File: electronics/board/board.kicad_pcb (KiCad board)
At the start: 2 copper layers, 196.2 x 40.6 mm, 82 parts, among them J1 Screw_Terminal_01x02, J10 Conn_01x02, J11 Conn_01x02, J12 Conn_01x02, J13 Conn_01x02, J14 Conn_01x02, J15 Conn_01x02, J16 Conn_01x02, J17 Conn_01x02, J18 Conn_01x02, J19 Conn_01x02, J2 Screw_Terminal_01x02, J20 Conn_01x02, J21 Conn_01x02, J22 Conn_01x02, J23 Conn_01x02, J3 AVR-ISP-6, J4 USB_B_Micro, J5 PD1, J6 Screw_Terminal_01x02, J7 Screw_Terminal_01x02, J8 Conn_01x02, J9 Conn_01x02, Q1 IRF7404, SW1 SW_Push_Open_Dual, U1 LMV358, U2 ATmega32U4-AU, U3 NCP1117-5.0_TO252, U4 ST485EBDR, U5 ULN2803A, U6 ULN2803A, Y1 Crystal 16MHz

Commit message: silk improved
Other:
- board text added: "- +"
- board text added: "12V solenoids"
- board text added: "12VDC"
- board text added: "B- A+"
- board text added: "Board Address"
- board text added: "MISO +5V SCK MOSI RST GND"
- board text added: "PD1"
- board text added: "RESET"
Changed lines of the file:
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@@
   (general
     (thickness 1.6)
-    (drawings 19)
+    (drawings 42)
     (tracks 842)
     (zones 0)
@@
     (tags "resistor handsolder")
     (attr smd)
-    (fp_text reference R1 (at 0 -1.65) (layer F.SilkS)
+    (fp_text reference R1 (at -0.025 1.66) (layer F.SilkS)
       (effects (font (size 1 1) (thickness 0.15)))
     )
@@
     (tags "resistor handsolder")
     (attr smd)
-    (fp_text reference R3 (at 0 -1.65 90) (layer F.SilkS)
+    (fp_text reference R3 (at -0.145 1.71 90) (layer F.SilkS)
       (effects (font (size 1 1) (thickness 0.15)))
     )
@@
     (tags "resistor handsolder")
     (attr smd)
-    (fp_text reference R8 (at 0 -1.65) (layer F.SilkS)
+    (fp_text reference R8 (at 0.025 1.71) (layer F.SilkS)
       (effects (font (size 1 1) (thickness 0.15)))
     )
@@
     (tags "resistor handsolder")
     (attr smd)
-    (fp_text reference RV1 (at 0 -1.65 180) (layer F.SilkS)
+    (fp_text reference RV1 (at 0.03 1.7135 180) (layer F.SilkS)
       (effects (font (size 1 1) (thickness 0.15)))
     )
@@
     (tags "resistor handsolder")
     (attr smd)
-    (fp_text reference RV2 (at 0 -1.65 180) (layer F.SilkS)
+    (fp_text reference RV2 (at -0.04 1.712 180) (layer F.SilkS)
       (effects (font (size 1 1) (thickness 0.15)))
     )
@@
     (tags "mounting hole 2.2mm no annular m2")
     (attr virtual)
-    (fp_text reference REF** (at 0 -3.2) (layer F.SilkS)
+    (fp_text reference REF** (at 0 -3.2) (layer F.SilkS) hide
       (effects (font (size 1 1) (thickness 0.15)))
     )
@@
     (tags "mounting hole 2.2mm no annular m2")
     (attr virtual)
-    (fp_text reference REF** (at 0 -3.2) (layer F.SilkS)
+    (fp_text reference REF** (at 0 -3.2) (layer F.SilkS) hide
       (effects (font (size 1 1) (thickness 0.15)))
     )
@@
     (pad 1 np_thru_hole circle (at 0 0) (size 2.2 2.2) (drill 2.2) (layers *.Cu *.Mask))
   )
+  (gr_line (start 134.37 17.28) (end 135.64 17.28) (layer F.SilkS) (width 0.2))
+  (gr_line (start 116.59 17.28) (end 134.37 17.28) (layer F.SilkS) (width 0.2))
+  (gr_text "Board\nAddress" (at 123.64 14.31) (layer F.SilkS)
+    (effects (font (size 1.5 1.5) (thickness 0.3)) (justify right))
+  )
+  (gr_poly (pts (xy 124.21 11.89) (xy 135.64 11.89) (xy 135.64 16.97) (xy 124.21 16.97)) (layer F.SilkS) (width 0.15))
+  (gr_text "MISO +5V\nSCK MOSI\nRST  GND" (at 155.55 12.19) (layer F.SilkS)
+    (effects (font (size 1 1) (thickness 0.25)) (justify left))
+  )
+  (gr_text PD1 (at 41.025 25.535) (layer B.SilkS)
+    (effects (font (size 1.5 1.5) (thickness 0.3)) (justify mirror))
+  )
+  (gr_text PD1 (at 41.66 24.9) (layer F.SilkS)
+    (effects (font (size 1.5 1.5) (thickness 0.3)))
+  )
+  (gr_text "12V solenoids" (at 98.81 36.33) (layer B.SilkS)
+    (effects (font (size 1.5 1.5) (thickness 0.3)) (justify mirror))
+  )
+  (gr_line (start 194.06 29.98) (end 2.925 29.98) (layer B.SilkS) (width 0.2))
+  (gr_text "PARAF board v1.1\nYoan Mollard" (at 126.75 21.725) (layer B.SilkS)
+    (effects (font (size 1.5 1.5) (thickness 0.3)) (justify mirror))
+  )
+  (gr_text RESET (at 190.25 4.58) (layer B.SilkS)
+    (effects (font (size 1.5 1.5) (thickness 0.3)) (justify mirror))
+  )
+  (gr_text RS485 (at 56.9 12.2) (layer B.SilkS)
+    (effects (font (size 1.5 1.5) (thickness 0.3)) (justify mirror))
+  )
+  (gr_text "B- A+" (at 63.25 8.39) (layer B.SilkS)
+    (effects (font (size 1.5 1.5) (thickness 0.3)) (justify mirror))
+  )
+  (gr_text "B- A+" (at 49.28 8.39) (layer B.SilkS)
+    (effects (font (size 1.5 1.5) (thickness 0.3)) (justify mirror))
+  )
+  (gr_line (start 68.33 13.47) (end 68.33 4.58) (layer B.SilkS) (width 0.2))
+  (gr_line (start 45.47 13.47) (end 68.33 13.47) (layer B.SilkS) (width 0.2))
+  (gr_line (start 45.47 4.58) (end 45.47 13.47) (layer B.SilkS) (width 0.2))
+  (gr_line (start 27.69 13.47) (end 27.69 4.58) (layer B.SilkS) (width 0.2))
+  (gr_line (start 4.83 13.47) (end 27.69 13.47) (layer B.SilkS) (width 0.2))
+  (gr_line (start 4.83 4.58) (end 4.83 13.47) (layer B.SilkS) (width 0.2))
+  (gr_text 12VDC (at 15.96 11.94) (layer B.SilkS)
+    (effects (font (size 1.5 1.5) (thickness 0.3)) (justify mirror))
+  )
+  (gr_text "-  +" (at 23.06 8.66) (layer B.SilkS)
+    (effects (font (size 1.5 1.5) (thickness 0.3)) (justify mirror))
+  )
+  (gr_text "-  +" (at 9.37 8.71) (layer B.SilkS)
+    (effects (font (size 1.5 1.5) (thickness 0.3)) (justify mirror))
+  )
   (gr_line (start 196.6 40.775) (end 0.385 40.775) (layer Edge.Cuts) (width 0.15))
   (gr_line (start 196.6 0.135) (end 196.6 40.775) (layer Edge.Cuts) (width 0.15))
@@
   (gr_line (start 44.84 14.08) (end 44.84 26.38) (layer F.SilkS) (width 0.2))
   (gr_line (start 38.72 14.08) (end 44.84 14.08) (layer F.SilkS) (width 0.2))
-  (gr_text "PARAF board v1.1\nYoan Mollard" (at 107.59 19.82) (layer F.SilkS)
+  (gr_text "PARAF board v1.1\nYoan Mollard" (at 106.145 20.595) (layer F.SilkS)
     (effects (font (size 1.5 1.5) (thickness 0.3)))
   )
@@
   (via (at 43.3 5.86) (size 0.8) (drill 0.4) (layers F.Cu B.Cu) (net 2))
   (via (at 43.15 11.42) (size 0.8) (drill 0.4) (layers F.Cu B.Cu) (net 2))
-  (via (at 58.01 11.64) (size 0.8) (drill 0.4) (layers F.Cu B.Cu) (net 2))
+  (via (at 57.535 9.66) (size 0.8) (drill 0.4) (layers F.Cu B.Cu) (net 2))
   (via (at 91.35 4.25) (size 0.8) (drill 0.4) (layers F.Cu B.Cu) (net 2))
   (via (at 113.85 15.33) (size 0.8) (drill 0.4) (layers F.Cu B.Cu) (net 2))
-  (via (at 119.64 15.16) (size 0.8) (drill 0.4) (layers F.Cu B.Cu) (net 2))
+  (via (at 119.54 14.43) (size 0.8) (drill 0.4) (layers F.Cu B.Cu) (net 2))
   (via (at 120.07 22.2) (size 0.8) (drill 0.4) (layers F.Cu B.Cu) (net 2))
   (via (at 129.5 20.61) (size 0.8) (drill 0.4) (layers F.Cu B.Cu) (net 2))

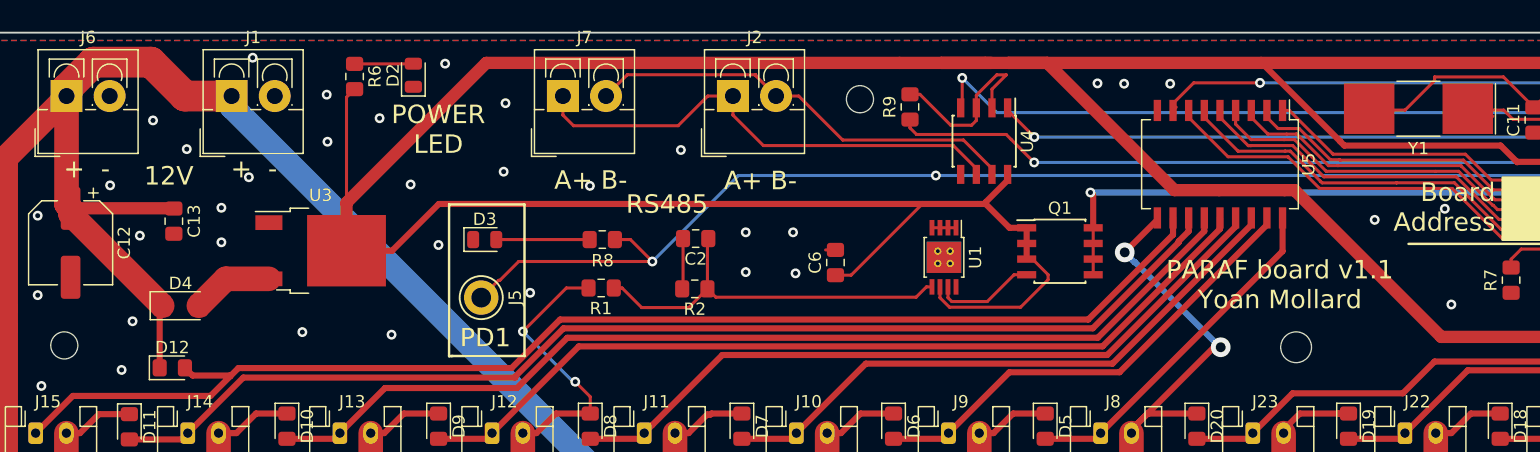
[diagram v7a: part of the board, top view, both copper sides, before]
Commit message: Improved silk
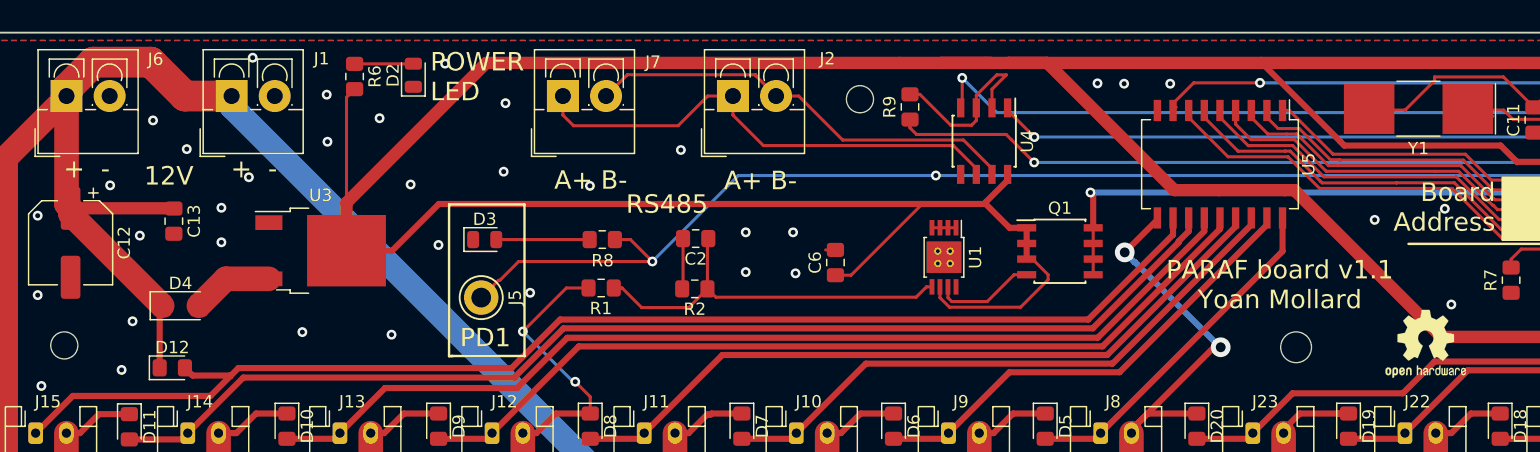
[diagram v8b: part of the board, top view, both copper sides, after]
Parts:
- added REF**: OSHW-Logo2_7.3x6mm_SilkScreen, Symbol:OSHW-Logo2_7.3x6mm_SilkScreen, F.Cu at (118.0, 25.4)
